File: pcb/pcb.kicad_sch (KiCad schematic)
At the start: 76 parts, among them J1 Conn_01x24, SW1 0, SW10 9, SW11 HYPHEN, SW12 CARET, SW13 YEN, SW14 @, SW15 [, SW16 SEMICOLON, SW17 COLON, SW18 ], SW19 COMMA, SW2 1, SW20 FULLSTOP, SW21 /, SW22 UNDERSCORE, SW23 A, SW24 B, SW25 C, SW26 D, SW27 E, SW28 F, SW29 G, SW3 2, SW30 H, SW31 I, SW32 J, SW33 K, SW34 L, SW35 M, SW36 N, SW37 O, SW38 P, SW39 Q, SW4 3, SW40 R, SW41 PAUSE, SW42 S, SW43 T, SW44 U, SW45 V, SW46 W, SW47 X, SW48 Y, SW49 Z, SW5 4, SW50 LSHIFT, SW51 CTRL, SW52 GRAPH, SW53 CAP, SW54 KANA, SW55 F1, SW56 F2, SW57 F3, SW58 RSHIFT, SW59 F4, SW6 5, SW60 F5, SW61 ESC, SW62 TAB, SW63 STOP, SW64 BS, SW65 SELECT, SW66 RETURN, SW67 SPACE, SW68 HOME, SW69 INS, SW7 6, SW70 DEL, SW71 LEFT, SW72 UP, SW73 DOWN, SW74 RIGHT, SW8 7, SW9 8

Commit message: Component placement
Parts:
- D1: footprint (none) -> Sony_Hit_Bit:LED
- J1: footprint (none) -> Sony_Hit_Bit:Connector
- SW1, SW10, SW11, SW12, SW13, SW14, SW15, SW16, SW17, SW18, SW19, SW2, SW20, SW21, SW22, SW23, SW24, SW25, SW26, SW27, SW28, SW29, SW3, SW30, SW31, SW32, SW33, SW34, SW35, SW36, SW37, SW38, SW39, SW4, SW40, SW41, SW42, SW43, SW44, SW45, SW46, SW47, SW48, SW49, SW5, SW50, SW51, SW52, SW53, SW54, SW55, SW56, SW57, SW58, SW59, SW6, SW60, SW61, SW62, SW63, SW64, SW65, SW66, SW67, SW68, SW69, SW7, SW70, SW71, SW72, SW73, SW74, SW8, SW9: footprint (none) -> Sony_Hit_Bit:Switch
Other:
- moved on the sheet: J1

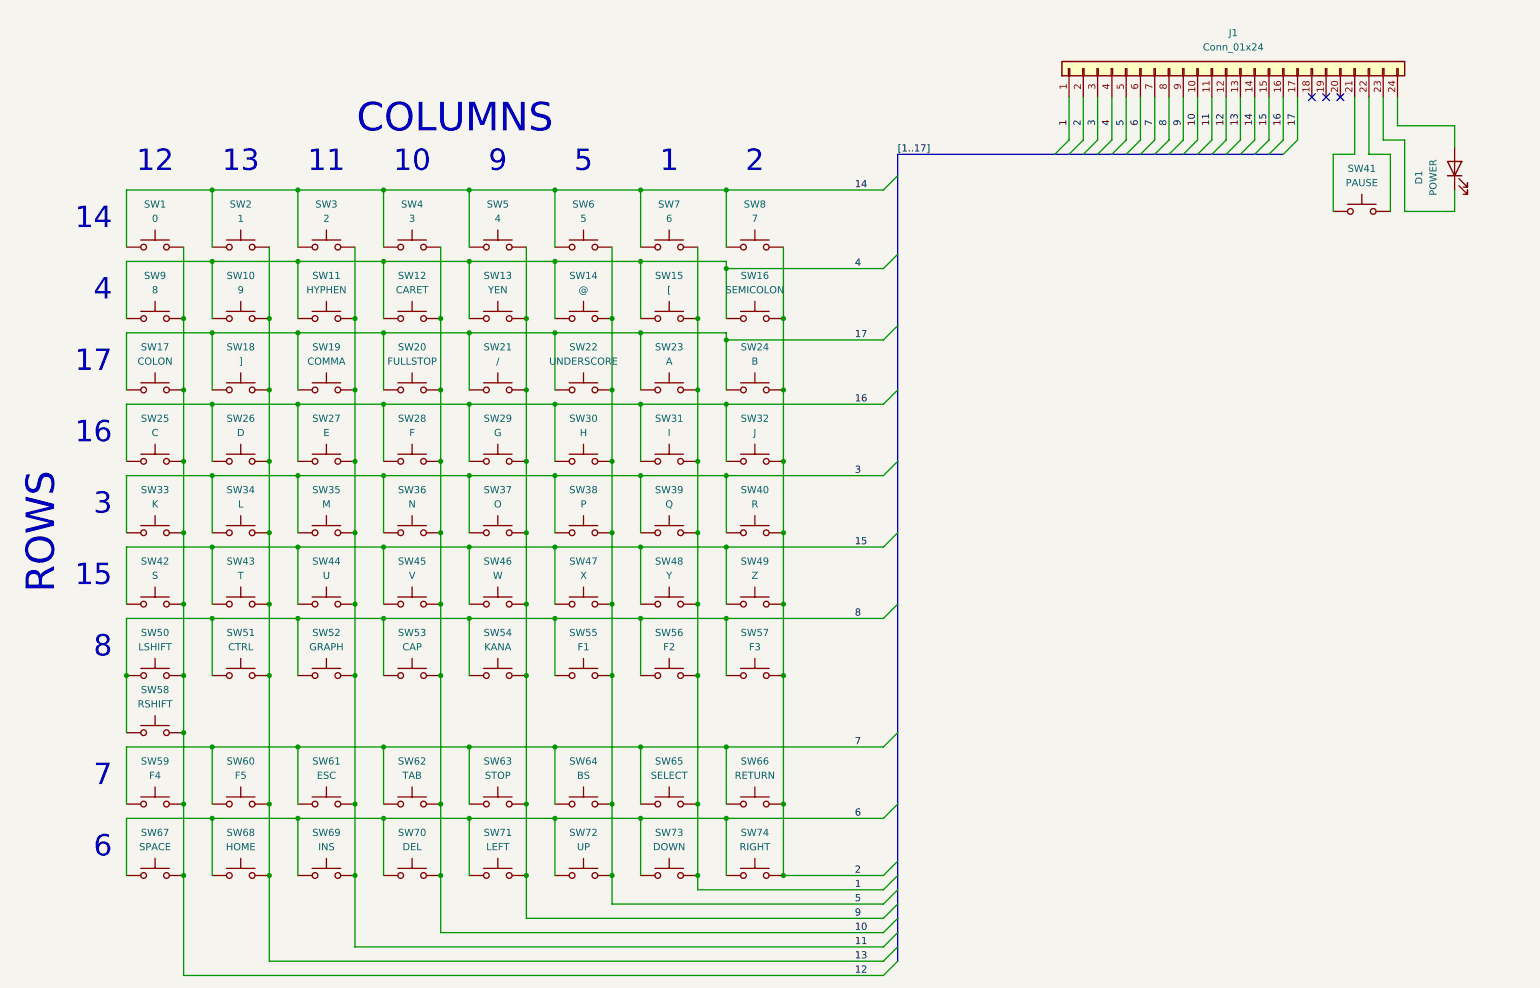
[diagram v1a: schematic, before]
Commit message: PCB fixing position errors and adding labels
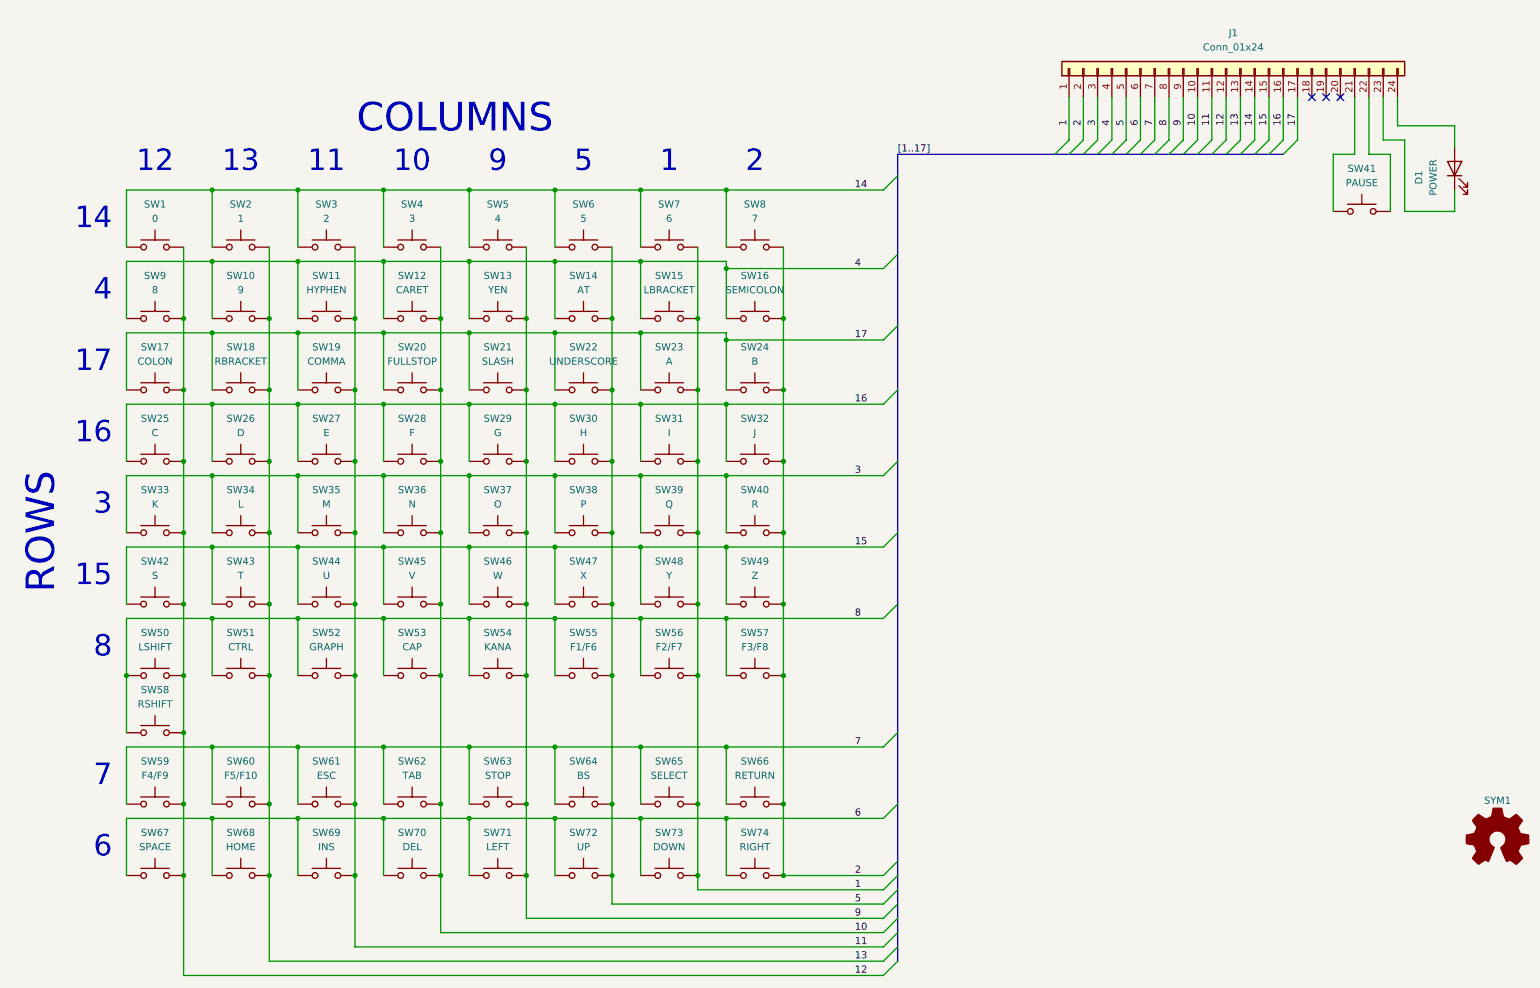
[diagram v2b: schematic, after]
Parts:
- added SYM1: Logo_Open_Hardware_Small, Symbol:OSHW-Logo_5.7x6mm_SilkScreen, symbol Graphic:Logo_Open_Hardware_Small
- SW14: value @ -> AT
- SW15: value [ -> LBRACKET
- SW18: value ] -> RBRACKET
- SW21: value / -> SLASH
- SW55: value F1 -> F1/F6
- SW56: value F2 -> F2/F7
- SW57: value F3 -> F3/F8
- SW59: value F4 -> F4/F9
- SW60: value F5 -> F5/F10
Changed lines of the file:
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@@
 	(title_block
 		(title "HB-F1 MSX Keyboard Membrane Schematic")
-		(date "2025-01-03")
+		(date "2025-01-07")
 		(rev "0.1")
 		(comment 1 "This source describes Open Hardware and is licensed under the CERN-OHL-W v2 or later.")
@@
 			)
 		)
-		(property "Value" "@"
+		(property "Value" "AT"
 			(at 114.3 59.69 0)
 			(effects
@@
 			)
 		)
-		(property "Value" "/"
+		(property "Value" "SLASH"
 			(at 99.06 72.39 0)
 			(effects
@@
 			)
 		)
-		(property "Value" "["
+		(property "Value" "LBRACKET"
 			(at 129.54 59.69 0)
 			(effects
@@
 			)
 		)
-		(property "Value" "F4"
+		(property "Value" "F4/F9"
 			(at 38.1 146.05 0)
 			(effects
@@
 			)
 		)
-		(property "Value" "]"
+		(property "Value" "RBRACKET"
 			(at 53.34 72.39 0)
 			(effects
@@
 			)
 		)
-		(property "Value" "F1"
+		(property "Value" "F1/F6"
 			(at 114.3 123.19 0)
 			(effects
@@
 			)
 		)
-		(property "Value" "F2"
+		(property "Value" "F2/F7"
 			(at 129.54 123.19 0)
 			(effects
@@
 	)
 	(symbol
+		(lib_id "Graphic:Logo_Open_Hardware_Small")
+		(at 276.86 157.48 0)
+		(unit 1)
+		(exclude_from_sim yes)
+		(in_bom no)
+		(on_board yes)
+		(dnp no)
+		(fields_autoplaced yes)
+		(property "Reference" "SYM1"
+			(at 276.86 150.495 0)
+			(effects
+				(font
+					(size 1.27 1.27)
+				)
+			)
+		)
+		(property "Value" "Logo_Open_Hardware_Small"
+			(at 276.86 163.195 0)
+			(effects
+				(font
+					(size 1.27 1.27)
+				)
+				(hide yes)
+			)
+		)
+		(property "Footprint" "Symbol:OSHW-Logo_5.7x6mm_SilkScreen"
+			(at 276.86 157.48 0)
+			(effects
+				(font
+					(size 1.27 1.27)
+				)
+				(hide yes)
+			)
+		)
+		(property "Datasheet" "~"
+			(at 276.86 157.48 0)
+			(effects
+				(font
+					(size 1.27 1.27)
+				)
+				(hide yes)
+			)
+		)
+		(property "Description" "Open Hardware logo, small"
+			(at 276.86 157.48 0)
+			(effects
+				(font
+					(size 1.27 1.27)
+				)
+				(hide yes)
+			)
+		)
+		(instances
+			(project ""
+				(path "/35b6008c-6b08-4e86-ab23-2043b1e9c38b"
+					(reference "SYM1")
+					(unit 1)
+				)
+			)
+		)
+	)
+	(symbol
 		(lib_id "Switch:SW_Push")
 		(at 129.54 163.83 0)
@@
 			)
 		)
-		(property "Value" "F3"
+		(property "Value" "F3/F8"
 			(at 144.78 123.19 0)
 			(effects
@@
 			)
 		)
-		(property "Value" "F5"
+		(property "Value" "F5/F10"
 			(at 53.34 146.05 0)
 			(effects

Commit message: PCB adding fiducials
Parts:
- added FID1, FID2: Fiducial, Fiducial:Fiducial_1mm_Mask2mm, symbol Mechanical:Fiducial
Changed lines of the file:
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@@
+	)
+	(symbol
+		(lib_id "Mechanical:Fiducial")
+		(at 243.84 160.02 0)
+		(unit 1)
+		(exclude_from_sim yes)
+		(in_bom no)
+		(on_board yes)
+		(dnp no)
+		(fields_autoplaced yes)
+		(property "Reference" "FID2"
+			(at 246.38 158.7499 0)
+			(effects
+				(font
+					(size 1.27 1.27)
+				)
+				(justify left)
+			)
+		)
+		(property "Value" "Fiducial"
+			(at 246.38 161.2899 0)
+			(effects
+				(font
+					(size 1.27 1.27)
+				)
+				(justify left)
+			)
+		)
+		(property "Footprint" "Fiducial:Fiducial_1mm_Mask2mm"
+			(at 243.84 160.02 0)
+			(effects
+				(font
+					(size 1.27 1.27)
+				)
+				(hide yes)
+			)
+		)
+		(property "Datasheet" "~"
+			(at 243.84 160.02 0)
+			(effects
+				(font
+					(size 1.27 1.27)
+				)
+				(hide yes)
+			)
+		)
+		(property "Description" "Fiducial Marker"
+			(at 243.84 160.02 0)
+			(effects
+				(font
+					(size 1.27 1.27)
+				)
+				(hide yes)
+			)
+		)
+		(instances
+			(project "pcb"
+				(path "/35b6008c-6b08-4e86-ab23-2043b1e9c38b"
+					(reference "FID2")
+					(unit 1)
+				)
+			)
+		)
 	)
 	(symbol
@@
 					(unit 1)
 				)
+			)
+		)
+	)
+	(symbol
+		(lib_id "Mechanical:Fiducial")
+		(at 243.84 153.67 0)
+		(unit 1)
+		(exclude_from_sim yes)
+		(in_bom no)
+		(on_board yes)
+		(dnp no)
+		(fields_autoplaced yes)
+		(property "Reference" "FID1"
+			(at 246.38 152.3999 0)
+			(effects
+				(font
+					(size 1.27 1.27)
+				)
+				(justify left)
+			)
+		)
+		(property "Value" "Fiducial"
+			(at 246.38 154.9399 0)
+			(effects
+				(font
+					(size 1.27 1.27)
+				)
+				(justify left)
+			)
+		)
+		(property "Footprint" "Fiducial:Fiducial_1mm_Mask2mm"
+			(at 243.84 153.67 0)
+			(effects
+				(font
+					(size 1.27 1.27)
+				)
+				(hide yes)
+			)
+		)
+		(property "Datasheet" "~"
+			(at 243.84 153.67 0)
+			(effects
+				(font
+					(size 1.27 1.27)
+				)
+				(hide yes)
+			)
+		)
+		(property "Description" "Fiducial Marker"
+			(at 243.84 153.67 0)
+			(effects
+				(font
+					(size 1.27 1.27)
+				)
+				(hide yes)
+			)
+		)
+		(instances
+			(project ""
+				(path "/35b6008c-6b08-4e86-ab23-2043b1e9c38b"
+					(reference "FID1")
+					(unit 1)
+				)

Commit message: Reviewing PCB and updating switch spacing
Changed soldermask layer on the connector to not be along the whole
trace. Reviewed the pinout of all the switches and confirmed they're
good. Reviewed the spacing of the switches and found errors, I have
moved them but am yet to reroute the traces. Updated the teardrops to be
curved.
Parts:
- removed SYM1: Logo_Open_Hardware_Small, Symbol:OSHW-Logo_5.7x6mm_SilkScreen, symbol Graphic:Logo_Open_Hardware_Small
- added FID3, FID4: Fiducial, Fiducial:Fiducial_1mm_Mask2mm, symbol Mechanical:Fiducial
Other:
- moved on the sheet: FID1, FID2
